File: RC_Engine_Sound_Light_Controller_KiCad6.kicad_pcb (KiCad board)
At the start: 2 copper layers, 70 x 39 mm, 36 parts, among them J1 RX, J10 RGB, J11 32, J12 CH1, J13 CH2, J14 CH3, J15 ESC, J16 CH4, J2 HeadL, J3 TailL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

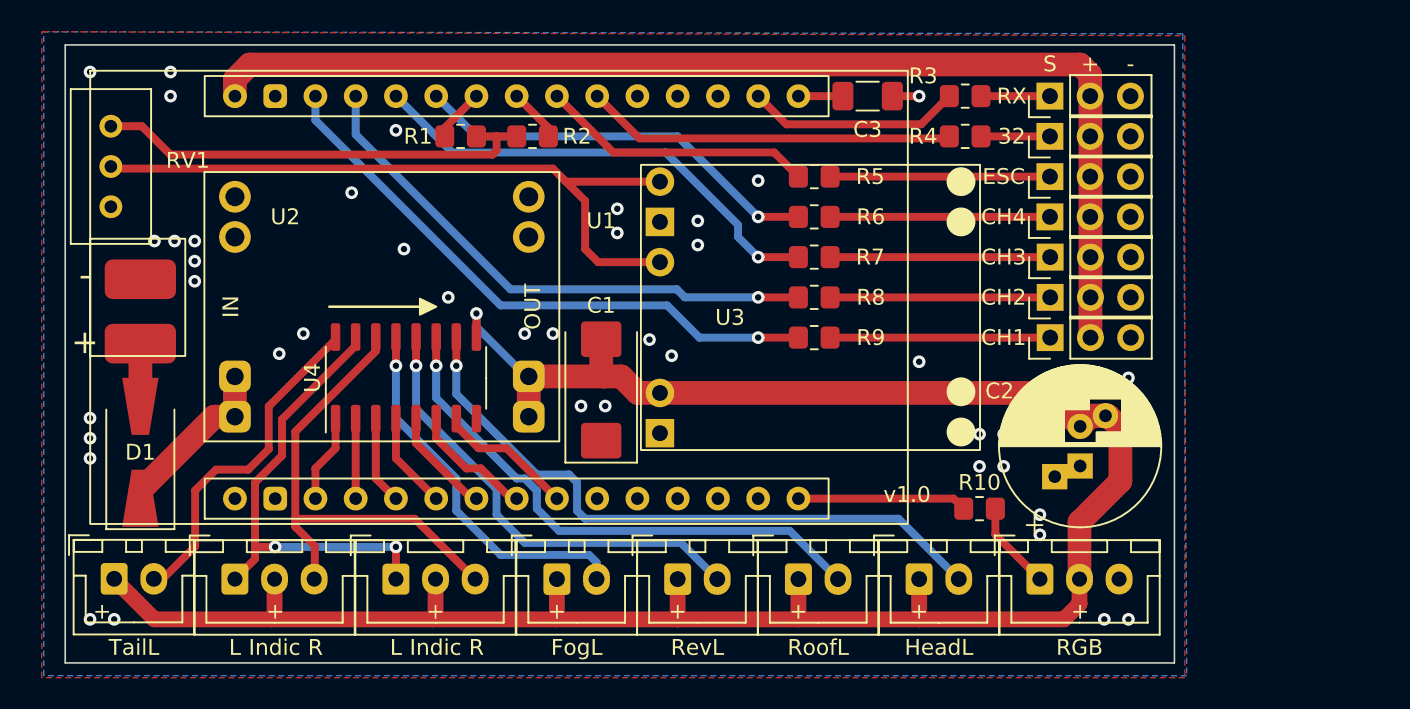
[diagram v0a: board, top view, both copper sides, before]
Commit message: Added VDD diode.
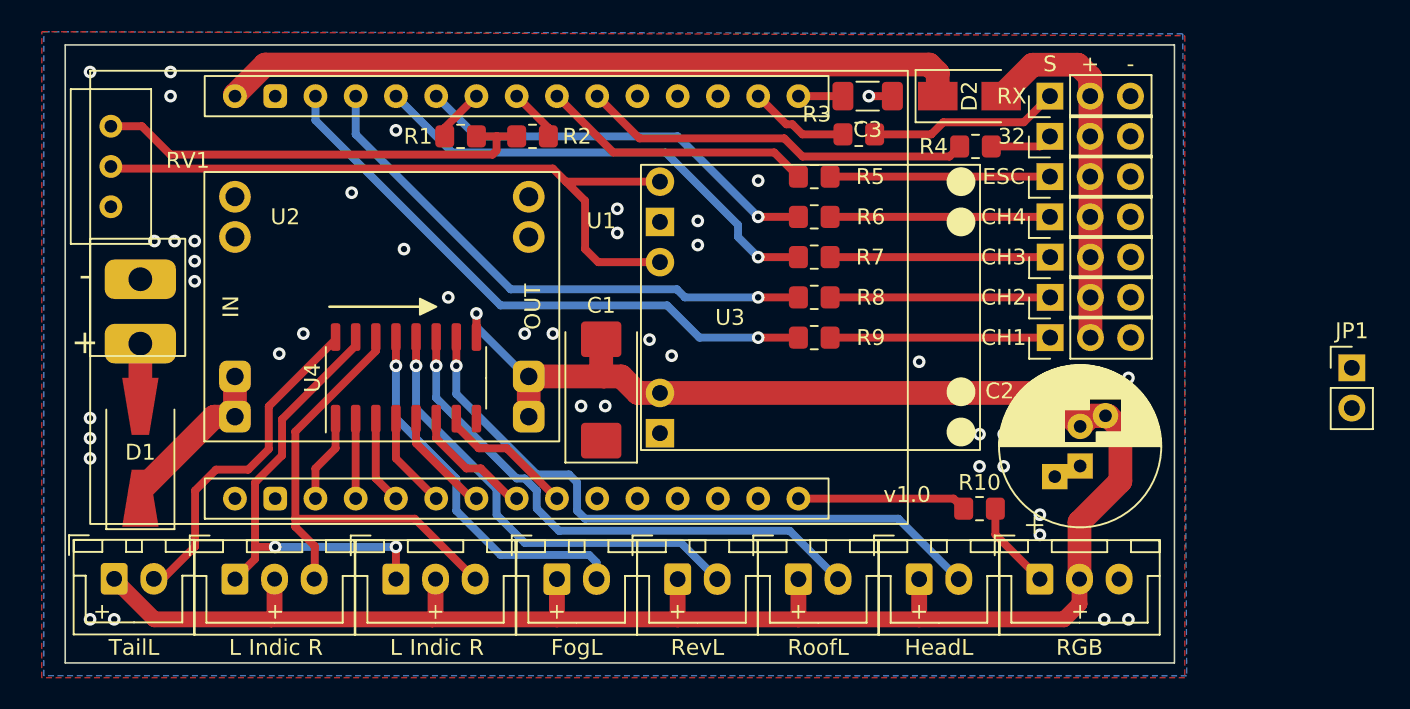
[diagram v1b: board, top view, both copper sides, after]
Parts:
- added D2: USB Supply Protection, Diode_SMD:D_SMA, F.Cu at (139.1, 49.5)
- added JP1: VDD +5V Bridge, Connector_PinHeader_2.54mm:PinHeader_1x02_P2.54mm_Vertical, F.Cu at (163.2, 66.7)
- D1: value D_Schottky -> Battery Polarity Protection
- moved R3 7.14 mm to (132.1, 51.9)
- moved R4 0.91 mm to (139.4, 52.7)
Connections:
- net Net-(C3-Pad1) renamed /EN_PIN
- net Net-(D1-Pad1) renamed /+12VIN
- net Net-(J1-Pad1) renamed /RX
- net Net-(J10-Pad1) renamed /RGB
- net Net-(J11-Pad1) renamed /PIN_32
- net Net-(J12-Pad1) renamed /CH1
- net Net-(J13-Pad1) renamed /CH2
- net Net-(J14-Pad1) renamed /CH3
- net Net-(J15-Pad1) renamed /ESC
- net Net-(J16-Pad1) renamed /CH4
- net Net-(R1-Pad2) renamed /AUDIO_JOINT
- net Net-(RV1-Pad2) renamed /AUDIO_INPUT
- U1 pad 30: VDD -> /VDD_IN
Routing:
- net VDD: track 72.3 -> 23.2 mm
- net /VDD_IN: track 0.00 -> 46.9 mm
- net /RX: track 4.35 -> 12.1 mm
- net D36: track 13.5 -> 6.35 mm
- net D32: track 23.2 -> 24.7 mm

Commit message: Removed EN cap, added USB diode.
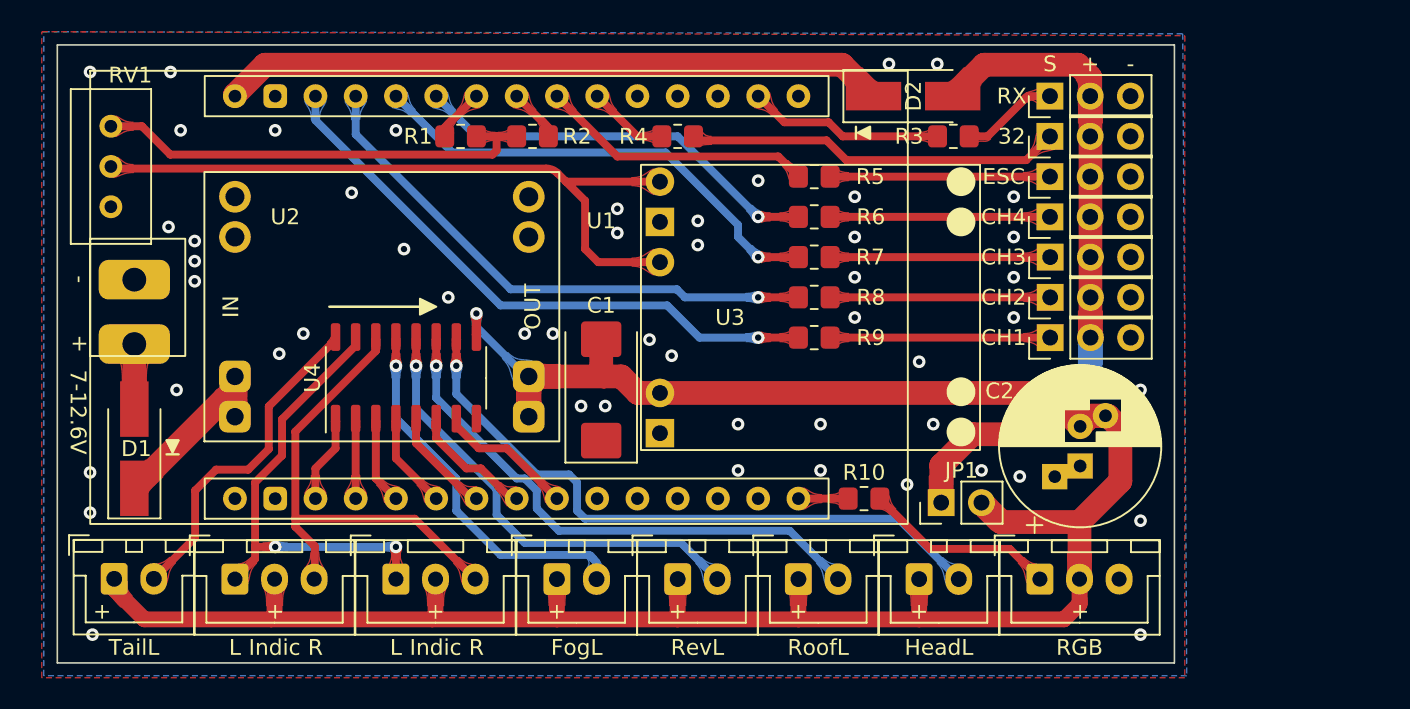
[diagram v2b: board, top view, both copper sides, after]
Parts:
- removed C3: 2.2µF, Capacitor_SMD:C_1206_3216Metric_Pad1.33x1.80mm_HandSolder
- D1: footprint Diode_SMD:D_SMA-SMB_Universal_Handsoldering -> Diode_SMD:D_SMA_Handsoldering
- D2: footprint Diode_SMD:D_SMA -> Diode_SMD:D_SMA_Handsoldering
- moved JP1 27.3 mm to (137.3, 75.2), turned to 90 degrees
- moved R4 18.8 mm to (120.7, 52.1)
- moved R10 7.32 mm to (132.4, 74.9)
- moved R3 5.97 mm to (138.0, 52.1)
- moved D2 3.56 mm to (135.5, 49.5)
- moved D1 0.44 mm to (86.4, 71.8)
- moved J8 0.38 mm to (86.4, 63.1)
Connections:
- U1 pad 16: /EN_PIN -> unconnected-(U1-Pad16)
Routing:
- net /PIN_32: track 3.96 -> 23.6 mm
- net D32: track 24.7 -> 5.13 mm
- net VDD: track 23.2 -> 42.6 mm, vias 0 -> 1
- net D23: track 10.7 -> 3.14 mm
- net +5V: track 144.2 -> 151.3 mm
- net /RGB: track 5.61 -> 12.2 mm
- net D36: track 6.35 -> 12.4 mm
- net /RX: track 12.1 -> 6.15 mm
- net /VDD_IN: track 46.9 -> 42.0 mm
- net /EN_PIN: track 2.60 -> 0.00 mm
- net GND: track 1.49 -> 0.00 mm, vias 43 -> 51
- net /+12VIN: track 10.4 -> 11.2 mm
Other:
- board size 70 x 39 mm -> 70.5 x 39 mm
- board text added: "7-12.6V"
- board text added: "Crawler PCB v1.0 2022-05-23 by neo2001"
- board text removed: "Crawler PCB v1.0 2022-05-13 by neo2001"
- board text removed: "v1.0"

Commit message: Rounded corners.
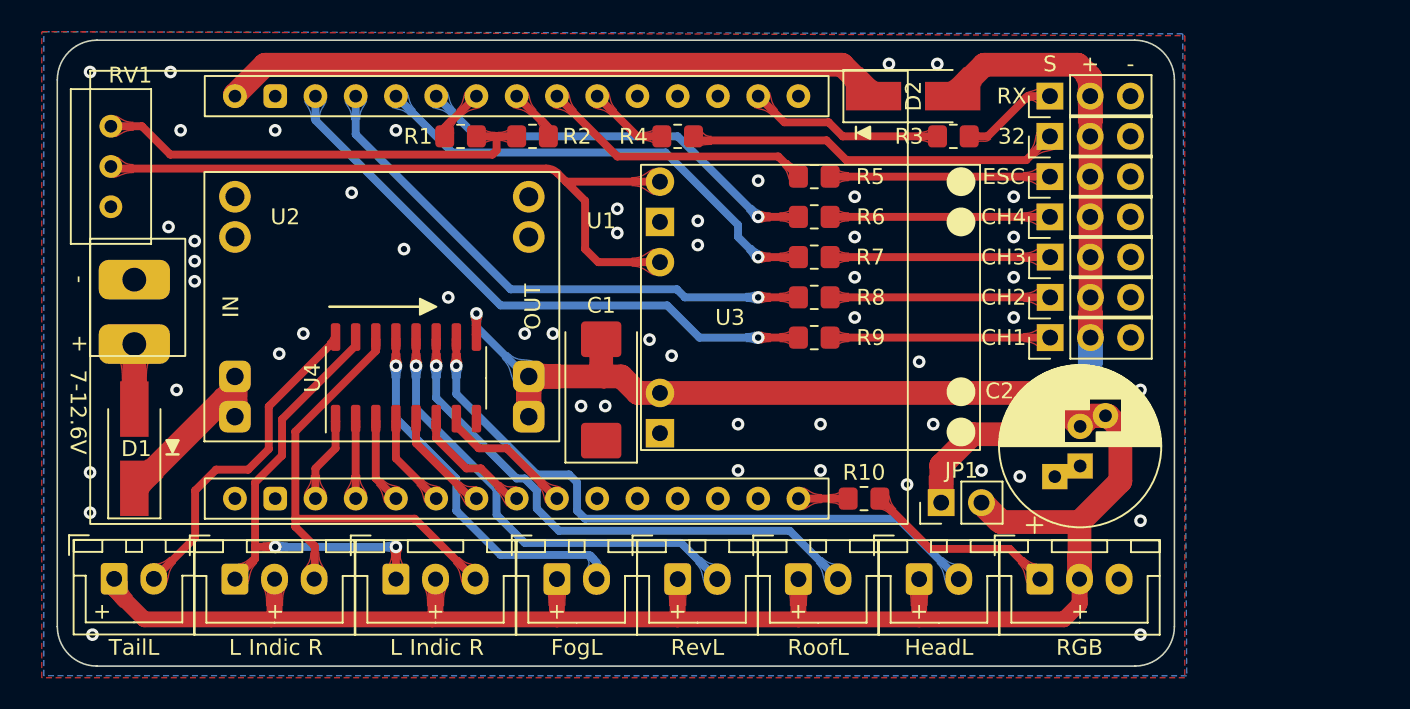
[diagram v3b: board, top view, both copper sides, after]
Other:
- board size 70.5 x 39 mm -> 70.5 x 39.5 mm
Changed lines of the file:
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@@
       (xy 132.7912 52.2224)
     ) (layer "F.SilkS") (width 0.15) (fill solid))
-  (gr_rect (start 81.5 46.3) (end 152 85.3) (layer "Edge.Cuts") (width 0.1) (fill none))
+  (gr_line (start 152 48.5) (end 152 83) (layer "Edge.Cuts") (width 0.1))
+  (gr_arc (start 149.5 46) (mid 151.267767 46.732233) (end 152 48.5) (layer "Edge.Cuts") (width 0.1))
+  (gr_line (start 84 46) (end 149.5 46) (layer "Edge.Cuts") (width 0.1))
+  (gr_arc (start 84 85.5) (mid 82.232233 84.767767) (end 81.5 83) (layer "Edge.Cuts") (width 0.1))
+  (gr_line (start 149.5 85.5) (end 84 85.5) (layer "Edge.Cuts") (width 0.1))
+  (gr_arc (start 152 83) (mid 151.267767 84.767767) (end 149.5 85.5) (layer "Edge.Cuts") (width 0.1))
+  (gr_line (start 81.5 83) (end 81.5 48.5) (layer "Edge.Cuts") (width 0.1))
+  (gr_arc (start 81.5 48.5) (mid 82.232233 46.732233) (end 84 46) (layer "Edge.Cuts") (width 0.1))
   (gr_text "More info: https://github.com/TheDIYGuy999/Rc_Engine_Sound_ESP32" (at 116.84 83.058) (layer "B.SilkS")
     (effects (font (size 1 1) (thickness 0.15)) (justify mirror))

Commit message: Changed +5V to VCC.
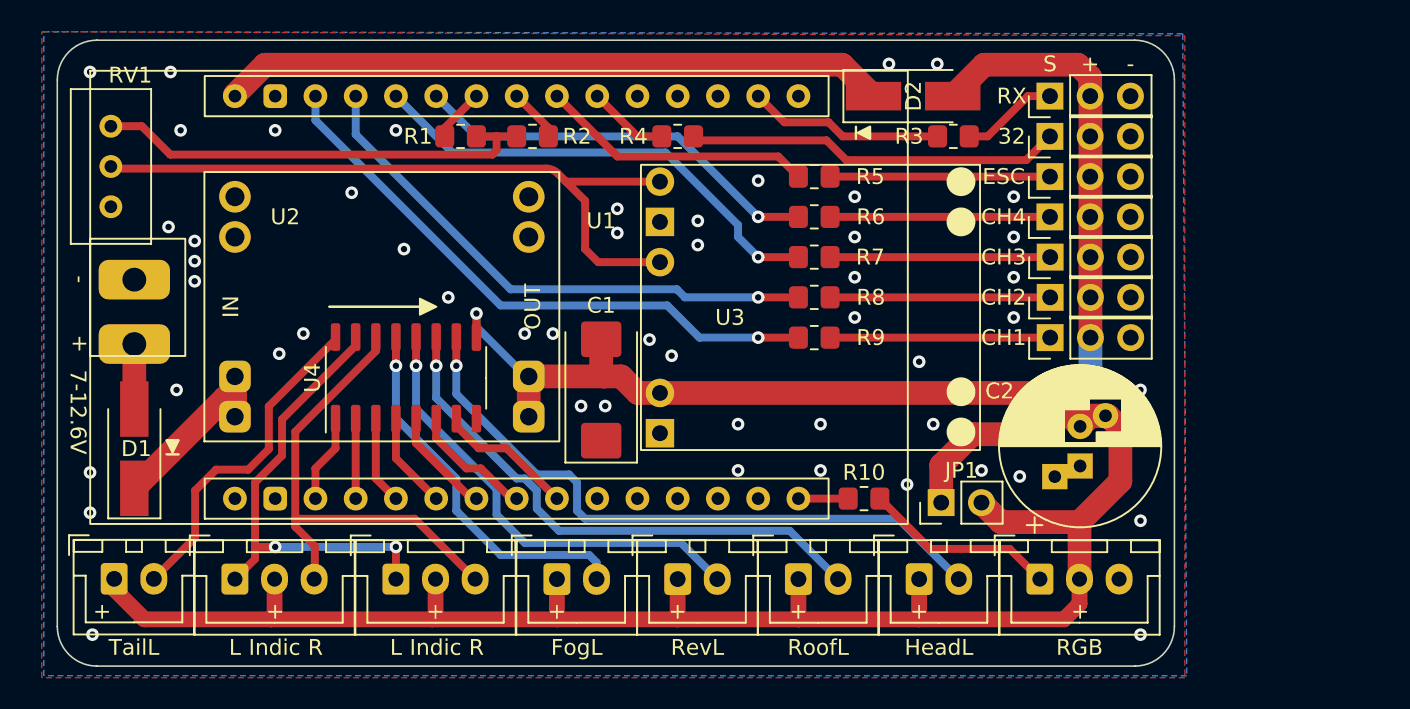
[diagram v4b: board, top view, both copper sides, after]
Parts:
- JP1: value VDD +5V Bridge -> VCC VDD Bridge
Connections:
- net +12V renamed +BATT
- net +5V renamed VCC
- net /+12VIN renamed Net-(D1-Pad1)
- net GND renamed -BATT

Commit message: Minor silkscreen improvements.
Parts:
- added REF**: DiodePolaritySilkscreenSymbol, cf:DiodePolaritySilkscreenSymbol, F.Cu at (88.9, 72.2)
- added REF**: DiodePolaritySilkscreenSymbol, cf:DiodePolaritySilkscreenSymbol, F.Cu at (131.9, 52.1)
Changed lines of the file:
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@@
     )
+  )
+  (footprint "cf:DiodePolaritySilkscreenSymbol" (layer "F.Cu")
+    (at 88.9 72.23)
+    (attr smd exclude_from_bom)
+    (fp_text reference "REF**" (at 0 -0.5 unlocked) (layer "F.SilkS") hide
+      (effects (font (size 1 1) (thickness 0.15)))
+    )
+    (fp_text value "DiodePolaritySilkscreenSymbol" (at 0 1 unlocked) (layer "F.Fab") hide
+      (effects (font (size 1 1) (thickness 0.15)))
+    )
+    (fp_text user "${REFERENCE}" (at 0 2.5 unlocked) (layer "F.Fab") hide
+      (effects (font (size 1 1) (thickness 0.15)))
+    )
+    (fp_line (start -0.508 0) (end 0.508 0) (layer "F.SilkS") (width 0.15))
+    (fp_poly (pts
+        (xy 0 -0.11176)
+        (xy -0.508 -1.12776)
+        (xy 0.508 -1.12776)
+      ) (layer "F.SilkS") (width 0.1) (fill solid))
   )
   (footprint "Capacitor_Tantalum_SMD:CP_EIA-7343-30_AVX-N_Pad2.25x2.55mm_HandSolder" (layer "F.Cu")
@@
       (rotate (xyz 0 0 -90))
     )
+  )
+  (footprint "cf:DiodePolaritySilkscreenSymbol" (layer "F.Cu")
+    (at 131.87012 52.07 -90)
+    (attr smd exclude_from_bom)
+    (fp_text reference "REF**" (at 0 -0.5 -90 unlocked) (layer "F.SilkS") hide
+      (effects (font (size 1 1) (thickness 0.15)))
+    )
+    (fp_text value "DiodePolaritySilkscreenSymbol" (at 0 1 -90 unlocked) (layer "F.Fab") hide
+      (effects (font (size 1 1) (thickness 0.15)))
+    )
+    (fp_text user "${REFERENCE}" (at 0 2.5 -90 unlocked) (layer "F.Fab") hide
+      (effects (font (size 1 1) (thickness 0.15)))
+    )
+    (fp_line (start -0.508 0) (end 0.508 0) (layer "F.SilkS") (width 0.15))
+    (fp_poly (pts
+        (xy 0 -0.11176)
+        (xy -0.508 -1.12776)
+        (xy 0.508 -1.12776)
+      ) (layer "F.SilkS") (width 0.1) (fill solid))
   )
   (footprint "cf:ESP32_DEVKITV1_30PIN" (layer "F.Cu")
@@
       ) (layer "B.SilkS") (width 0.01) (fill solid))
   )
-  (gr_poly
-    (pts
-      (xy 88.773 72.009)
-      (xy 88.392 71.247)
-      (xy 89.154 71.247)
-    ) (layer "F.SilkS") (width 0.15) (fill solid))
-  (gr_line (start 88.392 72.136) (end 89.154 72.136) (layer "F.SilkS") (width 0.15))
-  (gr_line (start 131.9022 51.4604) (end 131.9022 52.2224) (layer "F.SilkS") (width 0.15))
-  (gr_poly
-    (pts
-      (xy 132.0292 51.8414)
-      (xy 132.7912 51.4604)
-      (xy 132.7912 52.2224)
-    ) (layer "F.SilkS") (width 0.15) (fill solid))
+  (gr_circle (center 97.536 70.104) (end 98.044 70.104) (layer "F.SilkS") (width 0.15) (fill solid))
   (gr_line (start 152 48.5) (end 152 83) (layer "Edge.Cuts") (width 0.1))
   (gr_arc (start 149.5 46) (mid 151.267767 46.732233) (end 152 48.5) (layer "Edge.Cuts") (width 0.1))
@@
   )
   (gr_text "+" (at 120.65 82.042) (layer "F.SilkS")
+    (effects (font (size 1 1) (thickness 0.15)))
+  )
+  (gr_text "+" (at 115.81 66.58) (layer "F.SilkS")
     (effects (font (size 1 1) (thickness 0.15)))
   )
@@
   (segment (start 142.6464 53.5686) (end 144.145 52.07) (width 0.5) (layer "F.Cu") (net 34))
   (segment (start 131.2926 53.5686) (end 142.6464 53.5686) (width 0.5) (layer "F.Cu") (net 34))
-  (segment (start 121.7102 52.1462) (end 121.888 52.324) (width 0.5) (layer "F.Cu") (net 34))
   (segment (start 130.27 64.77) (end 144.16 64.77) (width 0.5) (layer "F.Cu") (net 35))
   (segment (start 130.27 62.23) (end 144.16 62.23) (width 0.5) (layer "F.Cu") (net 36))
@@
     )
   )
-  (group "" (id 20c87b46-1e28-48bc-ae1b-9dc49e7b7adc)
-    (members
-      6722cd8b-951e-4e19-b807-f5600c5539eb
-      746e2ba0-b1eb-4549-8965-2adada89be50
-    )
-  )
-  (group "" (id 50740c7a-e1e1-4129-b4cf-26f44a7e4cab)
-    (members
-      917391e8-039b-4c17-99c3-8658e49eeb68
-      c32c3e98-c2d5-490b-a67e-237ed8d27abd
-    )
-  )

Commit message: Moved pot slightly to the left.
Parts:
- moved RV1 0.40 mm to (84.5, 51.4)
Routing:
- net /AUDIO_INPUT: track 44.6 -> 45.2 mm
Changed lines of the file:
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@@
   )
   (footprint "Potentiometer_THT:Potentiometer_Bourns_3296W_Vertical" (layer "F.Cu")
-    (at 84.88 51.43 90)
+    (at 84.48 51.43 90)
     (descr "Potentiometer, vertical, Bourns 3296W, https://www.bourns.com/pdfs/3296.pdf")
     (tags "Potentiometer vertical Bourns 3296W")
@@
     (property "Sheetname" "")
     (attr through_hole)
-    (fp_text reference "RV1" (at 3.2208 1.226 180) (layer "F.SilkS")
+    (fp_text reference "RV1" (at 3.2208 1.226) (layer "F.SilkS")
       (effects (font (size 1 1) (thickness 0.15)))
     )
@@
   (segment (start 107.95 52.07) (end 105.41 49.53) (width 0.5) (layer "B.Cu") (net 45))
   (segment (start 128.27 74.93) (end 131.4102 74.93) (width 0.5) (layer "F.Cu") (net 47))
+  (segment (start 88.62712 53.21952) (end 86.8376 51.43) (width 0.5) (layer "F.Cu") (net 49))
+  (segment (start 108.966 53.21952) (end 88.62712 53.21952) (width 0.5) (layer "F.Cu") (net 49))
+  (segment (start 86.8376 51.43) (end 84.48 51.43) (width 0.5) (layer "F.Cu") (net 49))
+  (segment (start 109.22 52.07) (end 109.22 52.96552) (width 0.5) (layer "F.Cu") (net 49))
+  (segment (start 109.22 52.07) (end 110.49 52.07) (width 0.5) (layer "F.Cu") (net 49))
   (segment (start 109.22 52.96552) (end 108.966 53.21952) (width 0.5) (layer "F.Cu") (net 49))
-  (segment (start 108.966 53.21952) (end 88.62712 53.21952) (width 0.5) (layer "F.Cu") (net 49))
-  (segment (start 88.62712 53.21952) (end 86.8376 51.43) (width 0.5) (layer "F.Cu") (net 49))
-  (segment (start 86.8376 51.43) (end 84.88 51.43) (width 0.5) (layer "F.Cu") (net 49))
-  (segment (start 109.22 52.07) (end 110.49 52.07) (width 0.5) (layer "F.Cu") (net 49))
-  (segment (start 109.22 52.07) (end 109.22 52.96552) (width 0.5) (layer "F.Cu") (net 49))
   (segment (start 107.95 52.07) (end 109.22 52.07) (width 0.5) (layer "F.Cu") (net 49))
   (segment (start 114.808 59.182) (end 115.6335 60.0075) (width 0.5) (layer "F.Cu") (net 50))
   (segment (start 114.808 56.134) (end 114.808 59.182) (width 0.5) (layer "F.Cu") (net 50))
   (segment (start 115.6335 60.0075) (end 119.532 60.0075) (width 0.5) (layer "F.Cu") (net 50))
+  (segment (start 84.612 54.102) (end 112.361786 54.102) (width 0.5) (layer "F.Cu") (net 50))
+  (segment (start 113.6015 54.9275) (end 119.532 54.9275) (width 0.5) (layer "F.Cu") (net 50))
   (segment (start 113.068893 54.394893) (end 113.6015 54.9275) (width 0.5) (layer "F.Cu") (net 50))
-  (segment (start 113.6015 54.9275) (end 119.532 54.9275) (width 0.5) (layer "F.Cu") (net 50))
-  (segment (start 85.012 54.102) (end 112.361786 54.102) (width 0.5) (layer "F.Cu") (net 50))
+  (segment (start 84.48 53.97) (end 84.612 54.102) (width 0.5) (layer "F.Cu") (net 50))
   (segment (start 113.6015 54.9275) (end 114.808 56.134) (width 0.5) (layer "F.Cu") (net 50))
-  (arc (start 112.361786 54.102) (mid 112.744469 54.17812) (end 113.068893 54.394893) (width 0.5) (layer "F.Cu") (net 50))
+  (arc (start 112.361786 54.102) (mid 112.744469 54.178125) (end 113.068893 54.394893) (width 0.5) (layer "F.Cu") (net 50))
   (zone (net 2) (net_name "-BATT") (layer "F.Cu") (name "GND F") (hatch edge 0.508)
     (connect_pads (clearance 0.5))

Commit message: Corrected 5V caps silkscreen polarization.
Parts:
- moved C2 1.49 mm to (144.9, 71.9), turned to 0 degrees
- turned C1 to -90 degrees
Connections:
- net /VDD_IN renamed /VDD_VIN
- net Net-(D1-Pad1) renamed /BATT_VIN
- C1 pad 1: -BATT -> VCC
- C1 pad 2: VCC -> -BATT
- C2 pad 1: -BATT -> VCC
- C2 pad 2: VCC -> -BATT
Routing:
- net VCC: track 151.3 -> 141.4 mm
- net -BATT: vias 51 -> 53
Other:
- board size 70.5 x 39.5 mm -> 71.5 x 39.5 mm
- board text added: "Crawler PCB v1.1 2022-06-10 by neo2001"
- board text removed: "Crawler PCB v1.0 2022-05-23 by neo2001"
